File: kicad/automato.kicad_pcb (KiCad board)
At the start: 2 copper layers, 92.2 x 63.2 mm, 56 parts, among them J1 USB_C_Receptacle, J2 LiPo, J3 Conn_01x07_Male, J4 Screw_Terminal_01x20, Q1 Q_NPN_BCE, Q2 Q_NPN_BCE, Q3 DMG3415U, SW1 SW_Push, SW2 SW_Push, SW3 SW_SPDT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

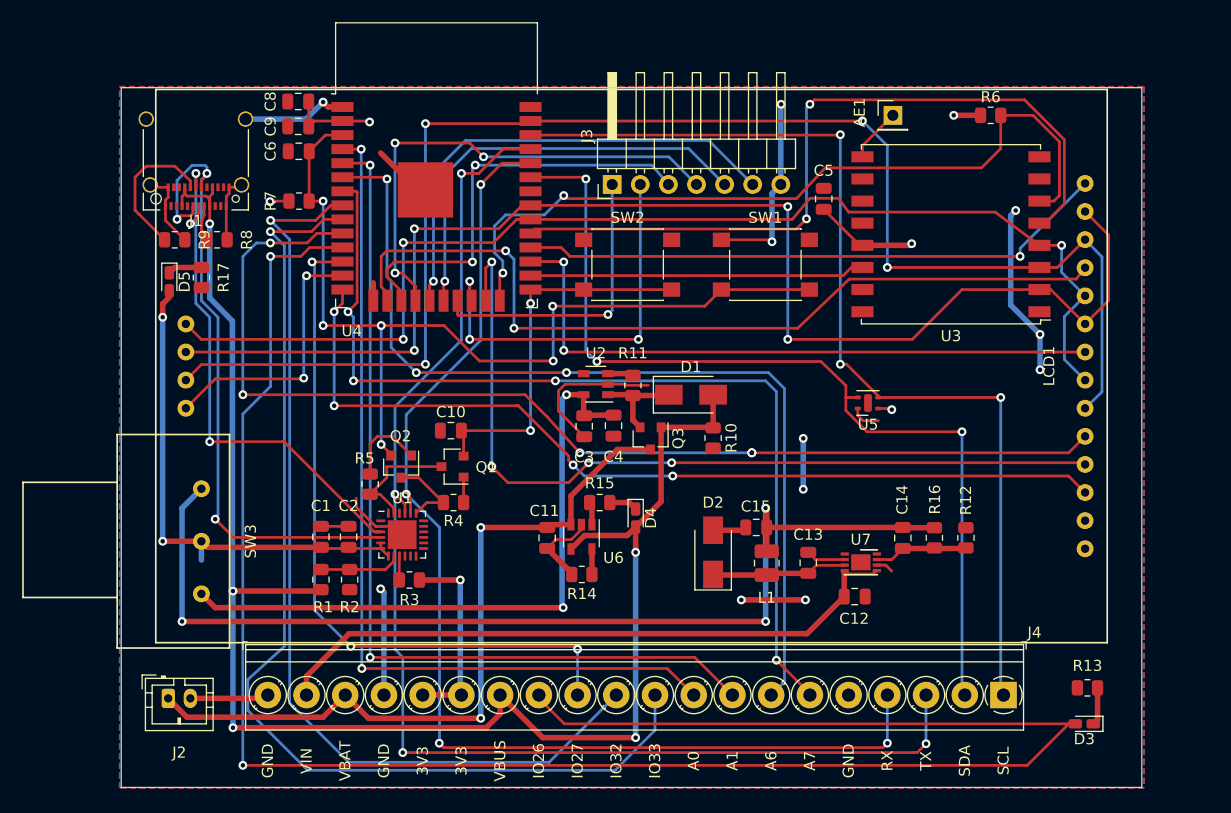
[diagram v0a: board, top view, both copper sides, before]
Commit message: layout: add mounting holes
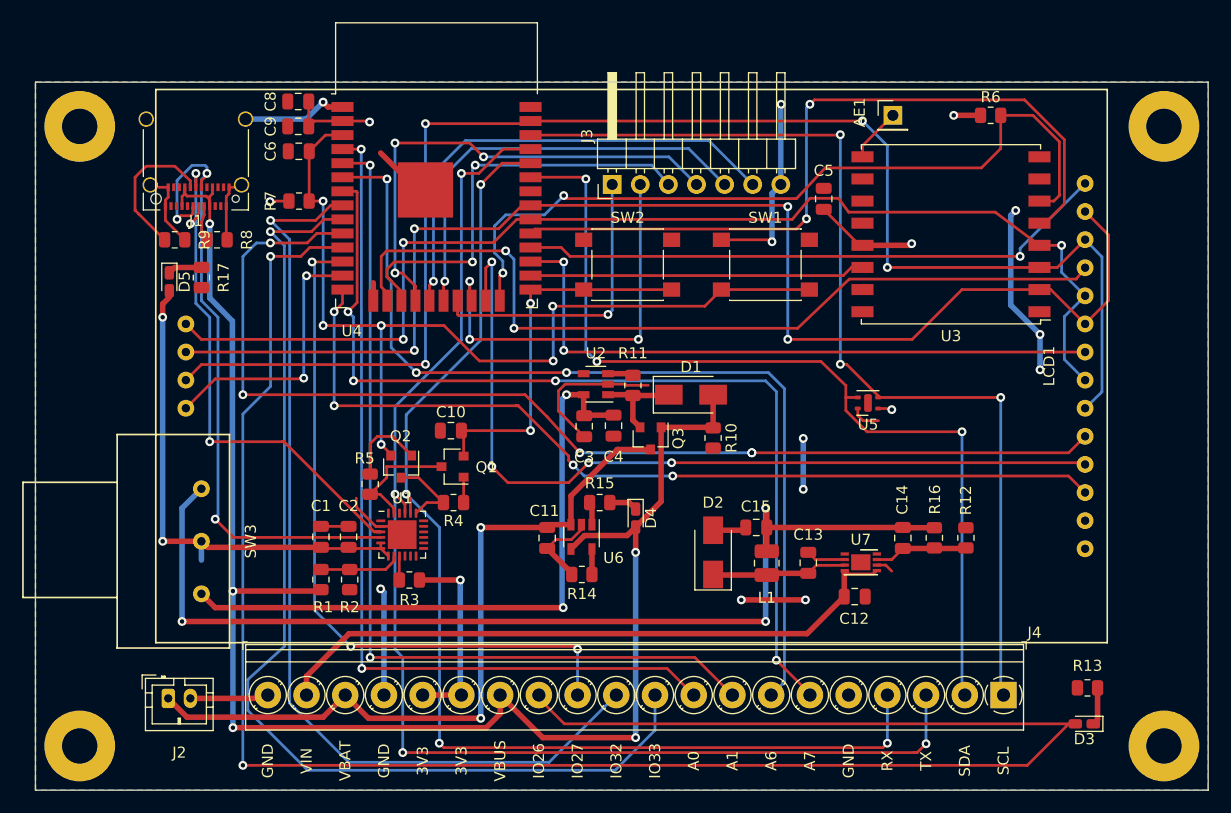
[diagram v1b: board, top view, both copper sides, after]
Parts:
- added REF**: MountingHole_3.2mm_M3_Pad, MountingHole:MountingHole_3.2mm_M3_Pad, F.Cu at (182.0, 117.0)
- added REF**: MountingHole_3.2mm_M3_Pad, MountingHole:MountingHole_3.2mm_M3_Pad, F.Cu at (182.0, 61.0)
- added REF**: MountingHole_3.2mm_M3_Pad, MountingHole:MountingHole_3.2mm_M3_Pad, F.Cu at (84.0, 117.0)
- added REF**: MountingHole_3.2mm_M3_Pad, MountingHole:MountingHole_3.2mm_M3_Pad, F.Cu at (84.0, 61.0)
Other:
- board size 92.2 x 63.2 mm -> 106 x 64 mm

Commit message: add I2C pull-ups
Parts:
- removed REF** (x4): MountingHole_3.2mm_M3_Pad, MountingHole:MountingHole_3.2mm_M3_Pad
- added R18: 4.7k, Resistor_SMD:R_0805_2012Metric, F.Cu at (163.8, 103.9)
- added R19: 4.7k, Resistor_SMD:R_0805_2012Metric, F.Cu at (167.4, 103.9)
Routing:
- net 3V3: track 92.2 -> 104.8 mm
- net I2C_SDA: track 83.8 -> 91.5 mm
- net I2C_SCL: track 91.5 -> 99.2 mm

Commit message: add test points
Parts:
- added REF**: MountingHole_3.2mm_M3_Pad, MountingHole:MountingHole_3.2mm_M3_Pad, F.Cu at (182.0, 61.0)
- added REF**: MountingHole_3.2mm_M3_Pad, MountingHole:MountingHole_3.2mm_M3_Pad, F.Cu at (182.0, 117.0)
- added REF**: MountingHole_3.2mm_M3_Pad, MountingHole:MountingHole_3.2mm_M3_Pad, F.Cu at (84.0, 117.0)
- added REF**: MountingHole_3.2mm_M3_Pad, MountingHole:MountingHole_3.2mm_M3_Pad, F.Cu at (84.0, 61.0)
- added TP1: TestPoint, TestPoint:TestPoint_Pad_D2.0mm, F.Cu at (180.5, 76.0)
- added TP2: TestPoint, TestPoint:TestPoint_Pad_D2.0mm, F.Cu at (180.5, 79.0)
- added TP3: TestPoint, TestPoint:TestPoint_Pad_D2.0mm, F.Cu at (180.5, 82.0)
- added TP4: TestPoint, TestPoint:TestPoint_Pad_D2.0mm, F.Cu at (180.5, 85.0)
- added TP5: TestPoint, TestPoint:TestPoint_Pad_D2.0mm, F.Cu at (147.0, 86.2)
- J1: footprint Connector_USB:USB_C_Receptacle_Amphenol_12401610E4-2A_CircularHoles -> automato-sensor:USB_C_Receptacle_Amphenol_12401610E4-2A_CircularHoles_nopads
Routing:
- net SPI_CLK: track 106.5 -> 122.9 mm
- net Net-(D1-Pad1): track 8.71 -> 19.9 mm
- net SPI_MOSI: track 133.2 -> 140.7 mm
- net DATA_CMD: track 101.4 -> 108.8 mm
- net SPI_MISO: track 120.3 -> 126.0 mm

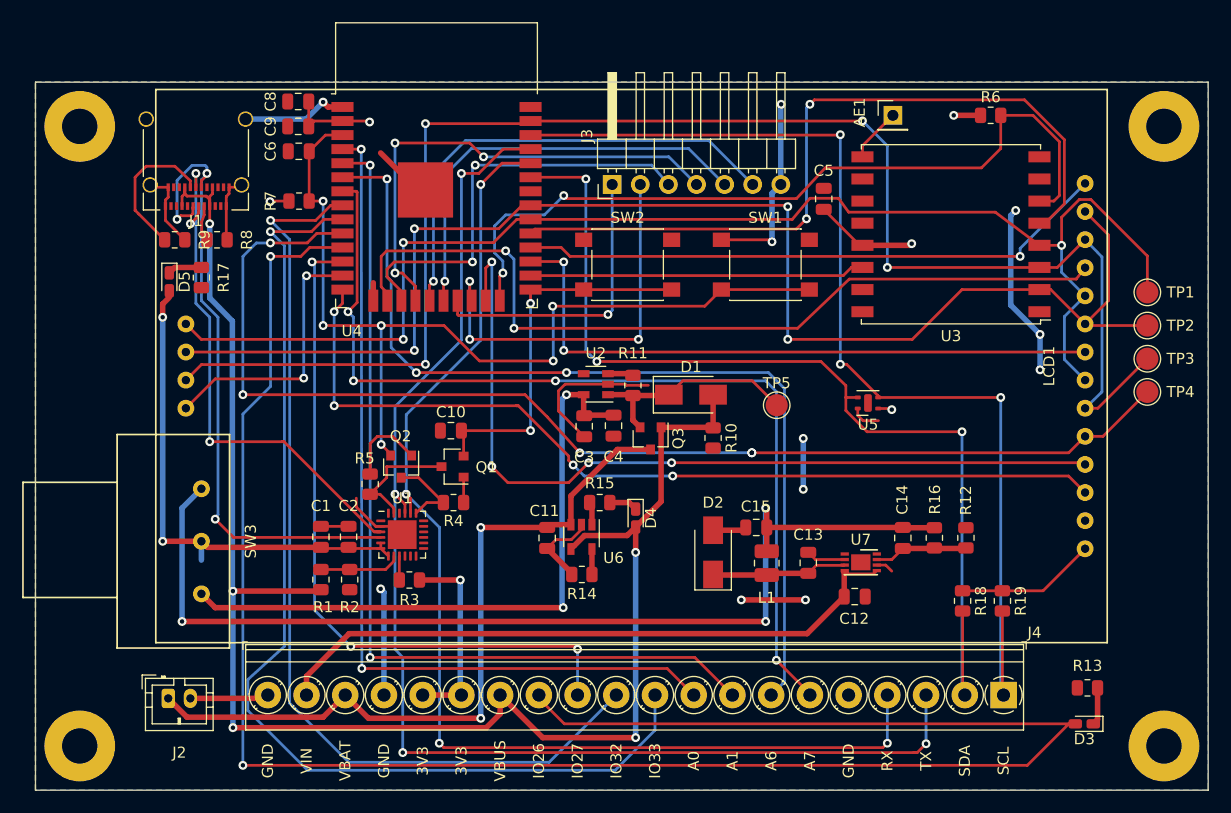
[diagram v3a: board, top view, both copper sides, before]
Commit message: CP2104: update layout
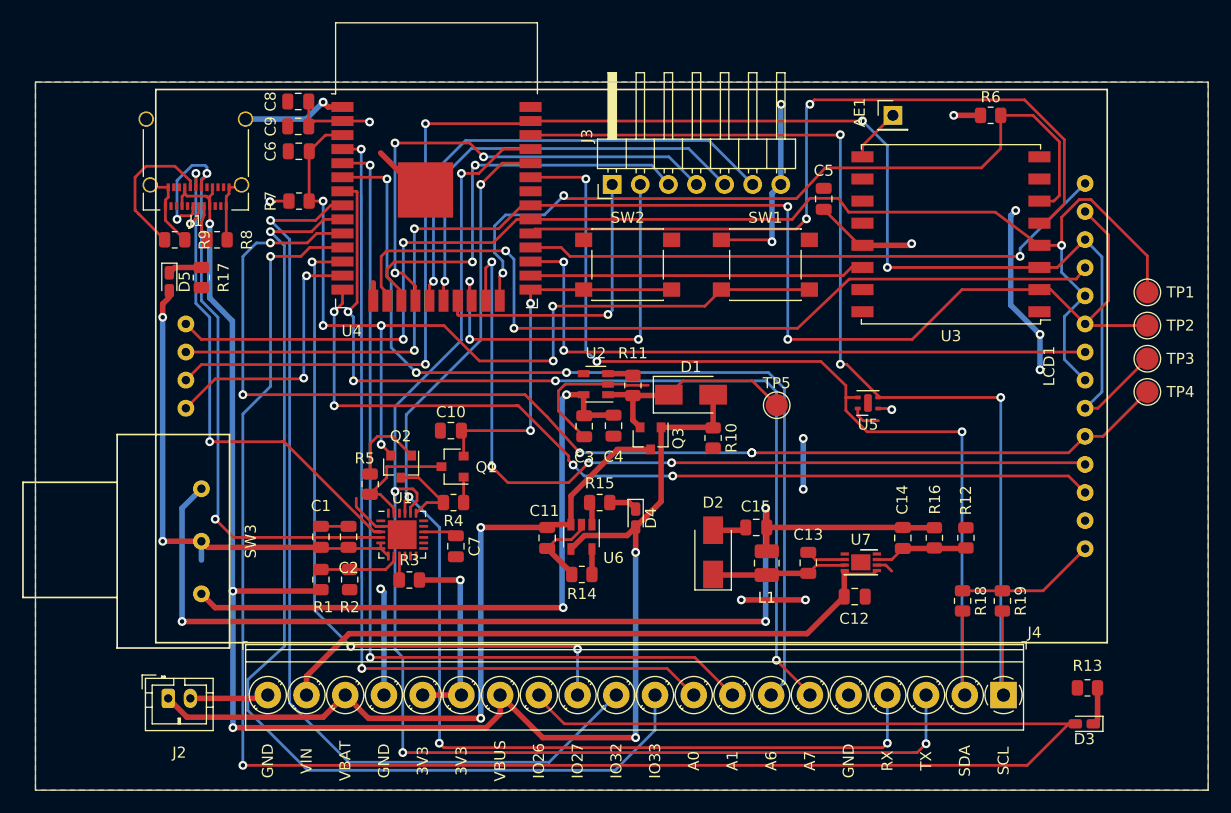
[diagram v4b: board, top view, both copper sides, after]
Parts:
- removed REF** (x4): MountingHole_3.2mm_M3_Pad, MountingHole:MountingHole_3.2mm_M3_Pad
- added C7: 4.7 uF, Capacitor_SMD:C_0805_2012Metric, F.Cu at (118.0, 99.0)
- R3: value 1k -> 4.7k
- U1: value CP2102N-A01-GQFN24 -> CP2104
- turned C2 to 90 degrees
- turned R3 to 180 degrees
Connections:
- C2 pad 1: GND -> 3V3
- C2 pad 2: 3V3 -> GND
- R3 pad 1: Net-(R3-Pad1) -> 3V3
- R3 pad 2: 3V3 -> Net-(R3-Pad2)
- U1 pad 16: (no net) -> Net-(C7-Pad1)
- U1 pad 20: RX -> TX
- U1 pad 21: TX -> RX
- U1 pad 9: Net-(R3-Pad1) -> Net-(R3-Pad2)
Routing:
- net Net-(C7-Pad1): track 0.00 -> 3.06 mm
- net TX: track 116.6 -> 118.8 mm
- net Net-(R3-Pad1): track 2.17 -> 0.00 mm
- net Net-(R3-Pad2): track 0.00 -> 2.17 mm

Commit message: layout: add back mounting holes
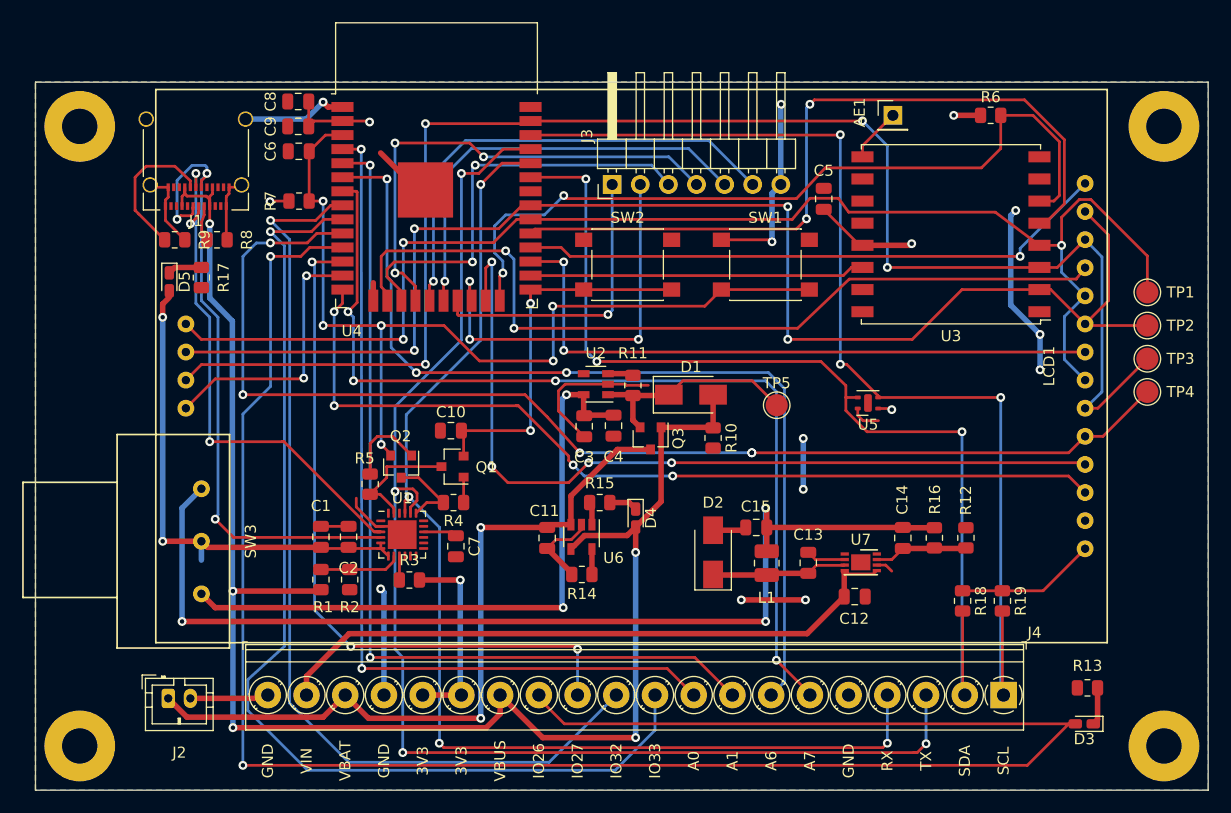
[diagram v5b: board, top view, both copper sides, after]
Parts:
- added REF**: MountingHole_3.2mm_M3_Pad, MountingHole:MountingHole_3.2mm_M3_Pad, F.Cu at (182.0, 61.0)
- added REF**: MountingHole_3.2mm_M3_Pad, MountingHole:MountingHole_3.2mm_M3_Pad, F.Cu at (182.0, 117.0)
- added REF**: MountingHole_3.2mm_M3_Pad, MountingHole:MountingHole_3.2mm_M3_Pad, F.Cu at (84.0, 117.0)
- added REF**: MountingHole_3.2mm_M3_Pad, MountingHole:MountingHole_3.2mm_M3_Pad, F.Cu at (84.0, 61.0)

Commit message: add silkscreen contributions from John
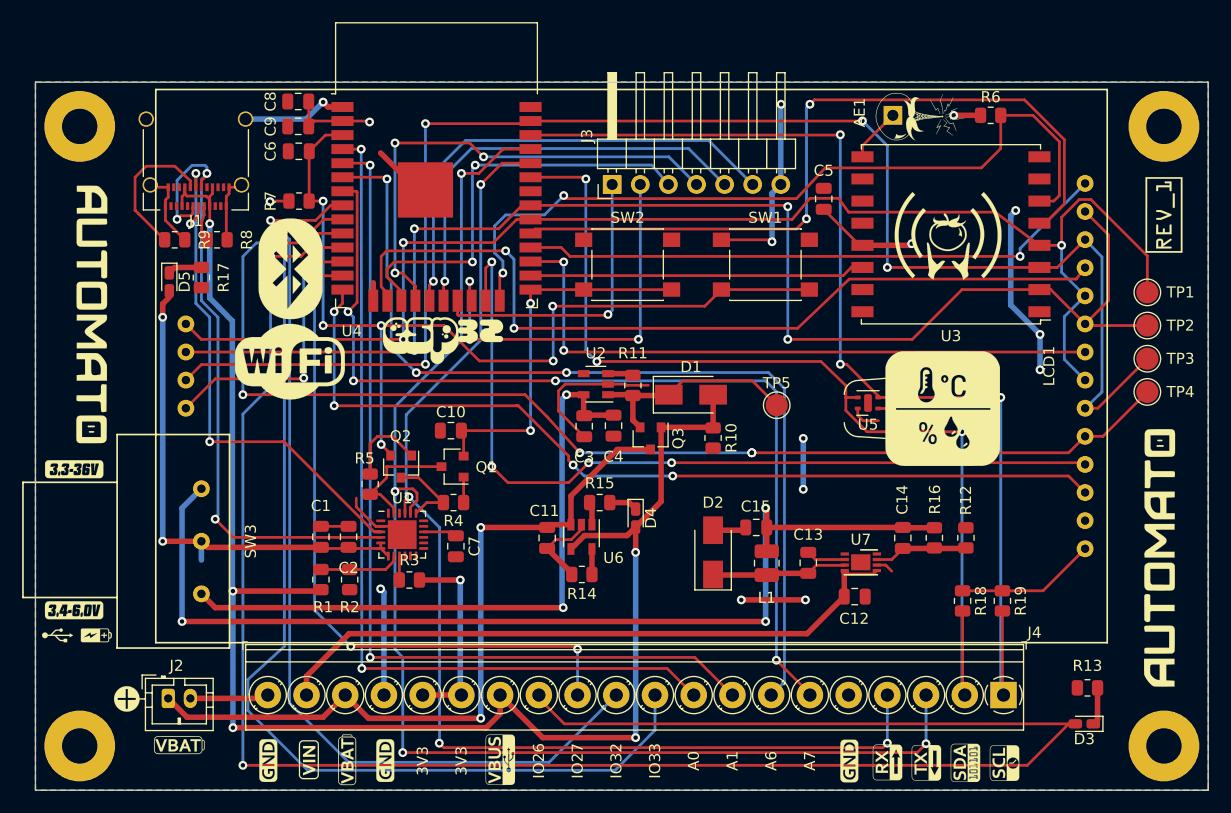
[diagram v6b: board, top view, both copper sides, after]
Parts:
- added G***: LOGO, logo:Version Number, F.Cu at (182.0, 69.0)
- added G***: LOGO, logo:Wifi Logo, F.Cu at (103.0, 82.2)
- added G***: LOGO, logo:USB Symbol, F.Cu at (122.0, 118.2)
- added G***: LOGO, logo:Temp-Humidity_Box, F.Cu at (162.0, 86.5)
- added G***: LOGO, logo:TX Symbol, F.Cu at (160.5, 118.5)
- added G***: LOGO, logo:SDA Symbol, F.Cu at (164.0, 118.5)
- added G***: LOGO, logo:SCL Symbol, F.Cu at (167.6, 118.6)
- added G***: LOGO, logo:RX Symbol, F.Cu at (157.0, 118.5)
- added G***: LOGO, logo:Logo_Simple_Small_NoText, F.Cu at (162.5, 70.9)
- added G***: LOGO, logo:GND, F.Cu at (153.6, 118.4)
- added G***: LOGO, logo:GND, F.Cu at (111.7, 118.3)
- added G***: LOGO, logo:Battery Symbol_V2, F.Cu at (85.5, 107.0)
- added G***: LOGO, logo:GND, F.Cu at (101.1, 118.3)
- added G***: LOGO, logo:ESP32__BubbleText, F.Cu at (116.8, 80.0)
- added G***: LOGO, logo:BlueTooth Logo, F.Cu at (103.1, 73.9)
- added G***: LOGO, logo:Automato_TextOnly_Small, F.Cu at (85.1, 78.0)
- added G***: LOGO, logo:Automato_TextOnly_Small, F.Cu at (181.6, 100.0)
- added G***: LOGO, logo:Automato Logo Mixer_BOLD_Neg, B.Cu at (132.8, 89.1)
- added G***: LOGO, logo:Antenna, F.Cu at (160.0, 60.1)
- added G***: LOGO, logo:USB_Symbol Only, F.Cu at (82.0, 107.0)
- added G***: LOGO, logo:VIN, F.Cu at (104.8, 118.2)
- added G***: LOGO, logo:VBAT, F.Cu at (108.2, 118.2)
- added G***: LOGO, logo:VIN Voltage Range, F.Cu at (83.5, 92.0)
- added G***: LOGO, logo:VBAT Voltage Range, F.Cu at (83.5, 104.8)
- added G***: LOGO, logo:VBAT, F.Cu at (93.0, 117.0)
- added G***: LOGO, logo:Positive Symbol, F.Cu at (88.2, 112.8)
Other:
- board text removed: "GND"
- board text removed: "RX"
- board text removed: "SCL"
- board text removed: "SDA"
- board text removed: "TX"
- board text removed: "VBAT"
- board text removed: "VBUS"
- board text removed: "VIN"

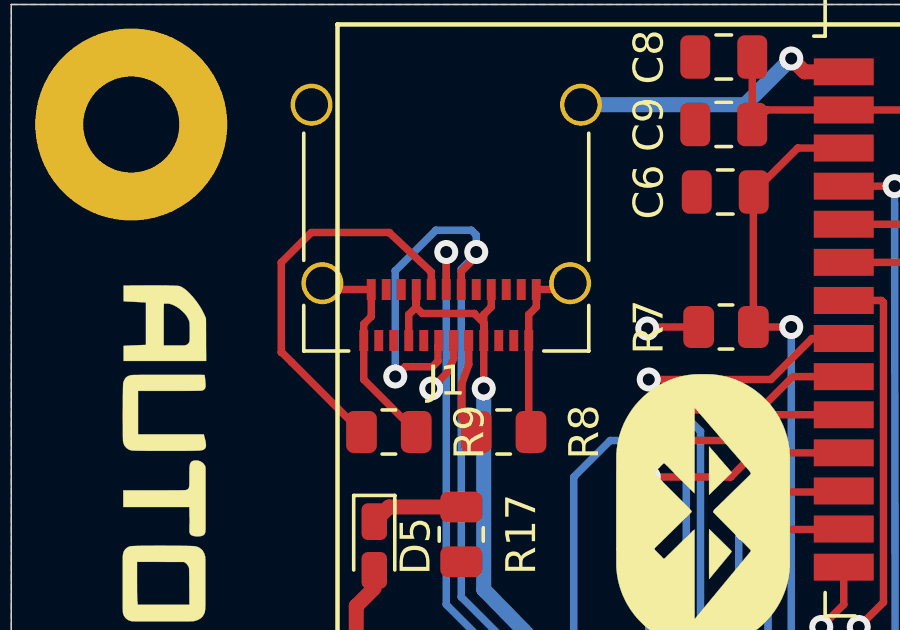
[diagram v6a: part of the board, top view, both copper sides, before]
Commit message: reduce pad width on USB-C receptacle to 0.29 mm
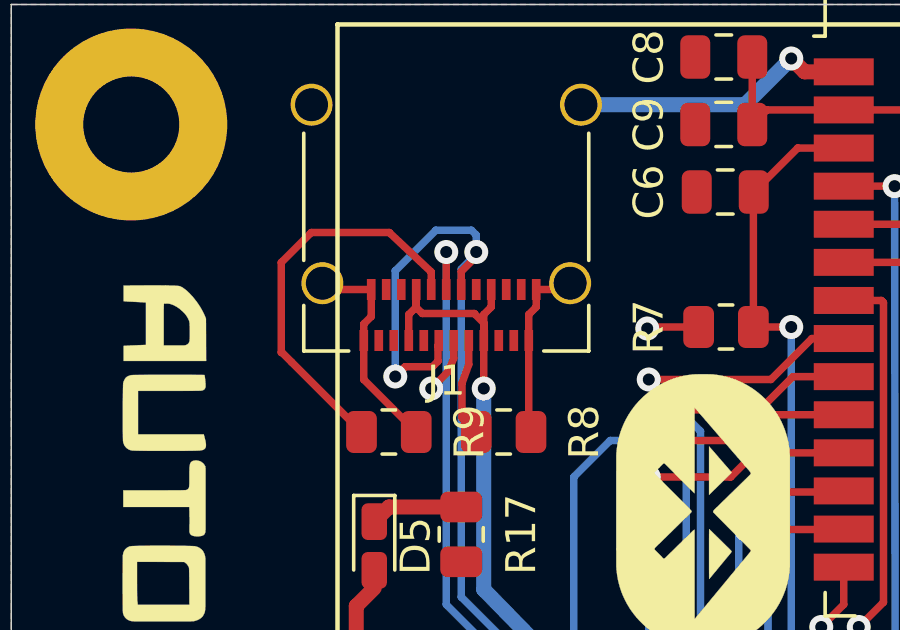
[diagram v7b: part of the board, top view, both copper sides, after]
